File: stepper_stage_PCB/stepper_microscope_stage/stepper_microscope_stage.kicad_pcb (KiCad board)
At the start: 2 copper layers, 131.5 x 158.8 mm, 22 parts, among them J1 Conn_01x04_Socket

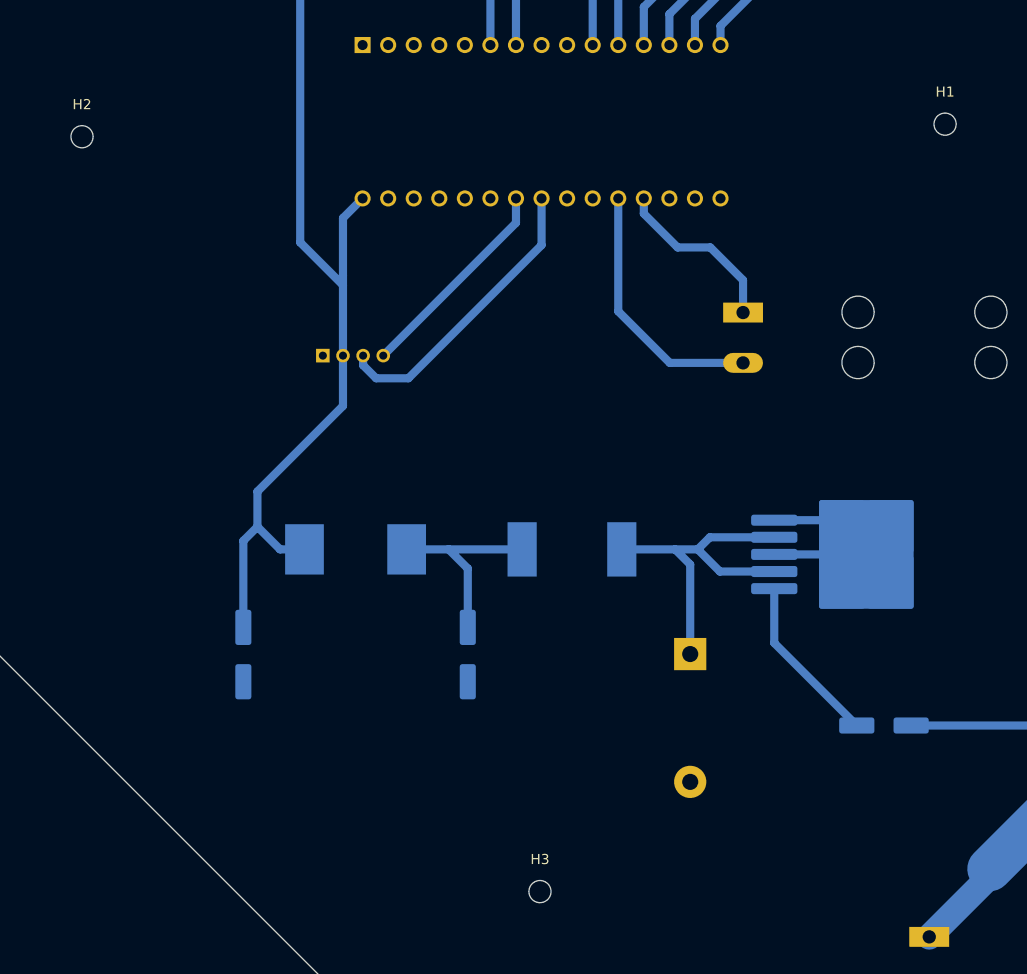
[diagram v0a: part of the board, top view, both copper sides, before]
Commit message: Updated mounting holes to be M4 instead of M2
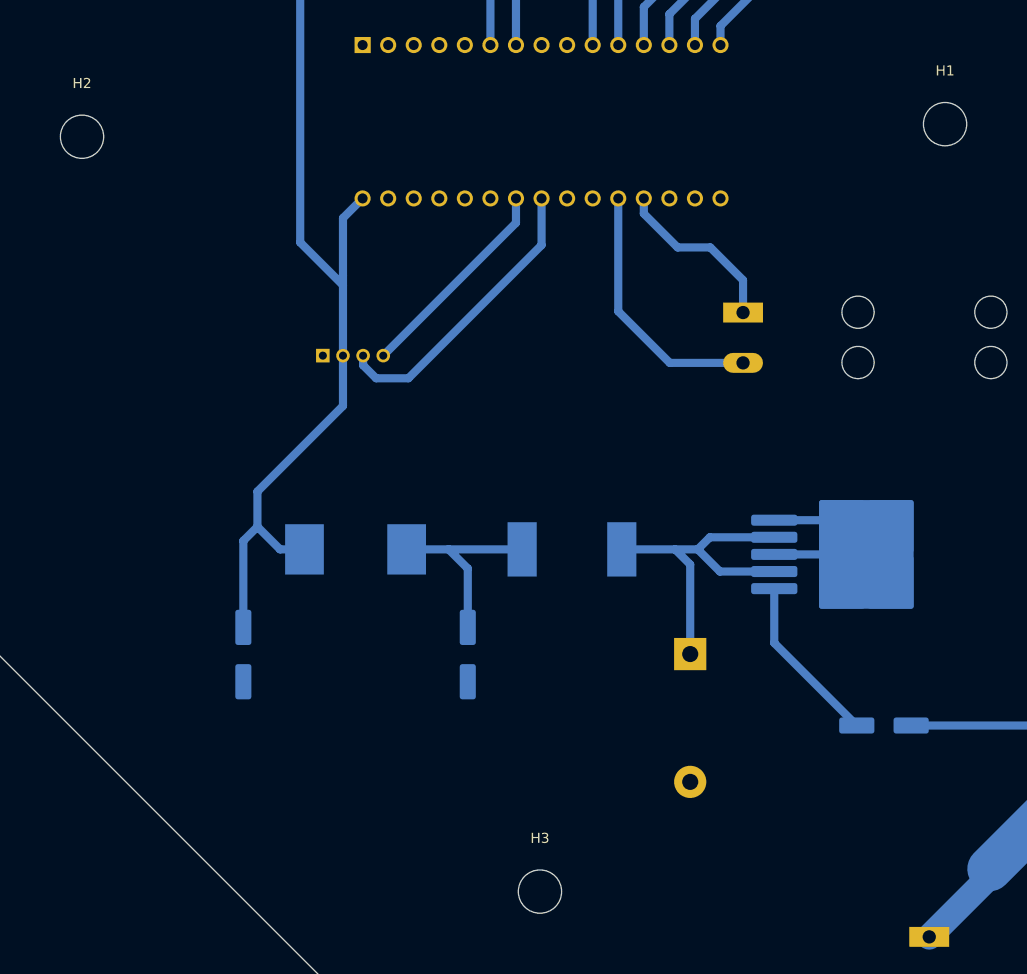
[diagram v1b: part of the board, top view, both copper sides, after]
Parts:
- H1, H2, H3: footprint MountingHole:MountingHole_2.2mm_M2 -> MountingHole:MountingHole_4.3mm_M4
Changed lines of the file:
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@@
   (net 33 "Net-(A1-A5)")
   (net 34 "Net-(C2-Pad1)")
-  (footprint "MountingHole:MountingHole_2.2mm_M2" (layer "F.Cu")
+  (footprint "MountingHole:MountingHole_4.3mm_M4" (layer "F.Cu")
     (at 132.5 83)
-    (descr "Mounting Hole 2.2mm, no annular, M2")
-    (tags "mounting hole 2.2mm no annular m2")
+    (descr "Mounting Hole 4.3mm, no annular, M4")
+    (tags "mounting hole 4.3mm no annular m4")
     (property "Sheetfile" "stepper_microscope_stage.kicad_sch")
     (property "Sheetname" "")
-    (property "ki_description" "Mounting Hole with connection")
+    (property "ki_description" "Mounting Hole without connection")
     (property "ki_keywords" "mounting hole")
     (attr exclude_from_pos_files)
-    (fp_text reference "H1" (at 0 -3.2) (layer "F.SilkS")
+    (fp_text reference "H1" (at 0 -5.3) (layer "F.SilkS")
         (effects (font (size 1 1) (thickness 0.15)))
     )
-    (fp_text value "MountingHole_Pad" (at 0 3.2) (layer "F.Fab")
+    (fp_text value "MountingHole_Pad" (at 0 5.3) (layer "F.Fab")
         (effects (font (size 1 1) (thickness 0.15)))
     )
@@
         (effects (font (size 1 1) (thickness 0.15)))
     )
-    (fp_circle (center 0 0) (end 2.2 0)
+    (fp_circle (center 0 0) (end 4.3 0)
       (stroke (width 0.15) (type solid)) (fill none) (layer "Cmts.User"))
-    (fp_circle (center 0 0) (end 2.45 0)
+    (fp_circle (center 0 0) (end 4.55 0)
       (stroke (width 0.05) (type solid)) (fill none) (layer "F.CrtYd"))
-    (pad "" np_thru_hole circle (at 0 0) (size 2.2 2.2) (drill 2.2) (layers "*.Cu" "*.Mask"))
+    (pad "" np_thru_hole circle (at 0 0) (size 4.3 4.3) (drill 4.3) (layers "*.Cu" "*.Mask"))
   )
-  (footprint "MountingHole:MountingHole_2.2mm_M2" (layer "F.Cu")
+  (footprint "MountingHole:MountingHole_4.3mm_M4" (layer "F.Cu")
     (at 46.75 84.25)
-    (descr "Mounting Hole 2.2mm, no annular, M2")
-    (tags "mounting hole 2.2mm no annular m2")
+    (descr "Mounting Hole 4.3mm, no annular, M4")
+    (tags "mounting hole 4.3mm no annular m4")
     (property "Sheetfile" "stepper_microscope_stage.kicad_sch")
     (property "Sheetname" "")
-    (property "ki_description" "Mounting Hole with connection")
+    (property "ki_description" "Mounting Hole without connection")
     (property "ki_keywords" "mounting hole")
     (attr exclude_from_pos_files)
-    (fp_text reference "H2" (at 0 -3.2) (layer "F.SilkS")
+    (fp_text reference "H2" (at 0 -5.3) (layer "F.SilkS")
         (effects (font (size 1 1) (thickness 0.15)))
     )
-    (fp_text value "MountingHole_Pad" (at 0 3.2) (layer "F.Fab")
+    (fp_text value "MountingHole_Pad" (at 0 5.3) (layer "F.Fab")
         (effects (font (size 1 1) (thickness 0.15)))
     )
@@
         (effects (font (size 1 1) (thickness 0.15)))
     )
-    (fp_circle (center 0 0) (end 2.2 0)
+    (fp_circle (center 0 0) (end 4.3 0)
       (stroke (width 0.15) (type solid)) (fill none) (layer "Cmts.User"))
-    (fp_circle (center 0 0) (end 2.45 0)
+    (fp_circle (center 0 0) (end 4.55 0)
       (stroke (width 0.05) (type solid)) (fill none) (layer "F.CrtYd"))
-    (pad "" np_thru_hole circle (at 0 0) (size 2.2 2.2) (drill 2.2) (layers "*.Cu" "*.Mask"))
+    (pad "" np_thru_hole circle (at 0 0) (size 4.3 4.3) (drill 4.3) (layers "*.Cu" "*.Mask"))
   )
-  (footprint "MountingHole:MountingHole_2.2mm_M2" (layer "F.Cu")
+  (footprint "MountingHole:MountingHole_4.3mm_M4" (layer "F.Cu")
     (at 92.25 159.25)
-    (descr "Mounting Hole 2.2mm, no annular, M2")
-    (tags "mounting hole 2.2mm no annular m2")
+    (descr "Mounting Hole 4.3mm, no annular, M4")
+    (tags "mounting hole 4.3mm no annular m4")
     (property "Sheetfile" "stepper_microscope_stage.kicad_sch")
     (property "Sheetname" "")
-    (property "ki_description" "Mounting Hole with connection")
+    (property "ki_description" "Mounting Hole without connection")
     (property "ki_keywords" "mounting hole")
     (attr exclude_from_pos_files)
-    (fp_text reference "H3" (at 0 -3.2) (layer "F.SilkS")
+    (fp_text reference "H3" (at 0 -5.3) (layer "F.SilkS")
         (effects (font (size 1 1) (thickness 0.15)))
     )
-    (fp_text value "MountingHole_Pad" (at 0 3.2) (layer "F.Fab")
+    (fp_text value "MountingHole_Pad" (at 0 5.3) (layer "F.Fab")
         (effects (font (size 1 1) (thickness 0.15)))
     )
@@
         (effects (font (size 1 1) (thickness 0.15)))
     )
-    (fp_circle (center 0 0) (end 2.2 0)
+    (fp_circle (center 0 0) (end 4.3 0)
       (stroke (width 0.15) (type solid)) (fill none) (layer "Cmts.User"))
-    (fp_circle (center 0 0) (end 2.45 0)
+    (fp_circle (center 0 0) (end 4.55 0)
       (stroke (width 0.05) (type solid)) (fill none) (layer "F.CrtYd"))
-    (pad "" np_thru_hole circle (at 0 0) (size 2.2 2.2) (drill 2.2) (layers "*.Cu" "*.Mask"))
+    (pad "" np_thru_hole circle (at 0 0) (size 4.3 4.3) (drill 4.3) (layers "*.Cu" "*.Mask"))
   )
   (footprint "Capacitor_SMD:CP_Elec_6.3x7.7" (layer "B.Cu")
